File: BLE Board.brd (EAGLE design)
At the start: 160 x 100 mm, 34 parts, among them IC1 TM4C123GH6PM, IC2 TPS6300, J1 SAMTEC-FTSH-105-01-X-DVJ, Q1 NX5032GA

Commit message: First arrangement of components
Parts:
- removed C4: 2.2uF, EE445L:C0402K
- removed J1: SAMTEC-FTSH-105-01-X-DVJ, SAMTEC-FTSH-105-01-X-DV:SAMTEC-FTSH-105-01-X-DV
- removed PC4, PF0, S1: (no value), EE445L:B3F-10XX
- removed Q1: NX5032GA, EE445L:NX5032GA
- removed R6: 10k, EE445L:R0402
- removed U$1: BGM220P, zyongye:BGM220P
- removed U$2: _SWITCH_SPDT_4.7, Z:_SWITCH_SPDT_4.7
- removed U$3: JTAG_SERIAL, Z:JTAG_SERIAL_PTH
- added BLE: BGM220P, zyongye:BGM220P
- added BLE-DEBUG: SAMTEC-FTSH-105-01-X-DVJ, SAMTEC-FTSH-105-01-X-DV:SAMTEC-FTSH-105-01-X-DV
- added C17, C19: 0.1uF, EE445L:C0402K
- added C18-T, C20-T: 4.7uF, EE445L:C0402K
- added C4-T: 2.2uF, EE445L:C0402K
- added CRYS: NX5032GA, EE445L:NX5032GA
- added JTAG: JTAG_SERIAL, Z:JTAG_SERIAL_PTH
- added ON/OFF: _SWITCH_SPDT_4.7, Z:_SWITCH_SPDT_4.7
- added R5: 10k, EE445L:R0402
- added RST, SW-PC4, SW-PF0: (no value), EE445L:B3F-10XX
- C13, C14, C16: value 0.01uF -> 10uF
- C15: value 0.01uF -> 0.1uF
- R3: value 1M -> 100
- moved R4 146.8 mm to (39.1, 49.5), flipped to the bottom
- moved DIS1 104.0 mm to (19.1, 43.2), flipped to the bottom
- moved C9 82.1 mm to (27.4, 25.9), turned to 315 degrees
- moved B1 79.4 mm to (31.0, 7.11), flipped to the bottom
- moved R1 78.4 mm to (39.6, 18.5), flipped to the bottom
- moved C12 75.5 mm to (24.8, 19.2), turned to 45 degrees
- moved C16 73.3 mm to (10.4, 7.37), flipped to the bottom, turned to 90 degrees
- moved C11 72.1 mm to (27.3, 21.7), turned to 225 degrees
- moved IC1 71.1 mm to (17.8, 30.5), turned to 225 degrees
- moved C15 69.2 mm to (11.7, 7.37), flipped to the bottom, turned to 90 degrees
- moved C1 68.7 mm to (8.89, 23.4), turned to 225 degrees
- moved C5 67.7 mm to (10.4, 21.8), turned to 45 degrees
- moved IC2 67.1 mm to (6.86, 3.81), flipped to the bottom, turned to 180 degrees
- moved C3 60.8 mm to (7.37, 24.9), turned to 225 degrees
- moved C14 60.3 mm to (3.30, 4.57), flipped to the bottom
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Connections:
- net +3V3: now also BLE.VDD, C17.2, C18-T.2, C19.1, C20-T.1, JTAG.3V3, SW-PC4.3, SW-PC4.4, SW-PF0.3, SW-PF0.4; no longer PC4.3, PC4.4, PF0.3, PF0.4, U$1.VDD, U$3.3V3
- net BAT: now also ON/OFF.P$2; no longer U$2.P$2
- net BGM_RST: now also BLE-DEBUG.3, BLE.RESET; no longer J1.3, U$1.RESET
- net GND: now also BLE-DEBUG.2, BLE.GND1, BLE.GND2, BLE.GND3, BLE.GND4, C17.1, C18-T.1, C19.2, C20-T.2, C4-T.2, JTAG.GND, R5.2, RST.3, RST.4; no longer C4.2, J1.2, R6.2, S1.3, S1.4, U$1.GND1, U$1.GND2, U$1.GND3, U$1.GND4, U$3.GND
- net IN: now also ON/OFF.P$1; no longer U$2.P$1
- net N$5: now also JTAG.5V; no longer U$3.5V
- net OSC0: now also CRYS.2; no longer Q1.2
- net OSC1: now also CRYS.1; no longer Q1.1
- net PF3: now also R5.1, SW-PF0.1, SW-PF0.2; no longer PF0.1, PF0.2, R6.1
- net PF4: now also SW-PC4.1, SW-PC4.2; no longer PC4.1, PC4.2
- net PTI_DATA: now also BLE-DEBUG.10, BLE.PC4; no longer J1.10, U$1.PC4
- net PTI_FRAME: now also BLE-DEBUG.9, BLE.PC5; no longer J1.9, U$1.PC5
- net RST: now also JTAG.RST, RST.1, RST.2; no longer S1.1, S1.2, U$3.RST
- net RXD: now also JTAG.RXD; no longer U$3.RXD
- net SWCLK: now also BLE-DEBUG.8, BLE.PA1; no longer J1.8, U$1.PA1
- net SWDIO: now also BLE-DEBUG.7, BLE.PA2; no longer J1.7, U$1.PA2
- net SWO: now also BLE-DEBUG.6, BLE.PA3; no longer J1.6, U$1.PA3
- net TCK: now also JTAG.TCK; no longer U$3.TCK
- net TDI: now also JTAG.TDI; no longer U$3.TDI
- net TDO: now also JTAG.TDO; no longer U$3.TDO
- net TMS: now also JTAG.TMS; no longer U$3.TMS
- net TXD: now also JTAG.TXD; no longer U$3.TXD
- net U1CTS: now also BLE.PA7; no longer U$1.PA7
- net U1RTS: now also BLE.PA8; no longer U$1.PA8
- net U1RX: now also BLE.PA5; no longer U$1.PA5
- net U1TX: now also BLE.PA6; no longer U$1.PA6
- net VDD: now also BLE-DEBUG.1; no longer J1.1
- net VDDC: now also C4-T.1; no longer C4.1
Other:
- board size 160 x 100 mm -> 51.3 x 67 mm

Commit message: revised BLE layout
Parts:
- moved BLE-DEBUG 27.7 mm to (-0.76, 52.8), flipped to the bottom
- moved C18-T 22.9 mm to (20.6, 49.8), flipped to the bottom
- moved C17 17.0 mm to (15.2, 49.8), flipped to the bottom
- moved BLE 12.5 mm to (24.4, 59.9), flipped to the bottom, turned to 0 degrees
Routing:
- added copper zone on layer 16, net N$2

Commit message: First traces
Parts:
- moved C17 2.42 mm to (12.8, 49.9)
- moved C18-T 2.42 mm to (23.0, 49.9), turned to 0 degrees
- moved C3 1.48 mm to (8.13, 23.6)
- moved C1 1.48 mm to (9.65, 22.1)
- moved C5 1.31 mm to (11.0, 20.7)
- moved R5 0.85 mm to (39.2, 35.8)
- moved R4 0.65 mm to (39.2, 48.9), turned to 180 degrees
- moved BLE-DEBUG 0.51 mm to (-0.76, 53.3)
- moved L1 0.51 mm to (6.86, 8.13)
- moved R2 0.18 mm to (12.3, 19.7)
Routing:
- net GND: track 0.00 -> 314.2 mm, vias 0 -> 18
- net +3V3: track 0.00 -> 196.1 mm, vias 0 -> 11
- net TXD: track 0.00 -> 70.2 mm
- net RXD: track 0.00 -> 67.8 mm
- net RST: track 0.00 -> 55.9 mm, vias 0 -> 1
- net SWCLK: track 0.00 -> 52.5 mm, vias 0 -> 4
- net BGM_RST: track 0.00 -> 49.8 mm, vias 0 -> 4
- net PF4: track 0.00 -> 48.2 mm, vias 0 -> 3
- net SWO: track 0.00 -> 46.0 mm, vias 0 -> 2
- net SWDIO: track 0.00 -> 43.3 mm, vias 0 -> 2
- net PF3: track 0.00 -> 39.7 mm, vias 0 -> 1
- net TFT_CS: track 0.00 -> 38.6 mm
- net PTI_FRAME: track 0.00 -> 31.8 mm, vias 0 -> 2
- net SCLK: track 0.00 -> 30.0 mm
- net U1CTS: track 0.00 -> 28.4 mm, vias 0 -> 3
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
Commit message: Fix all errors
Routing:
- net N$4: track 3.92 -> 3.34 mm
- removed copper zone on layer 16, net N$2
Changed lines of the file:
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@@
 <hole x="-3.429" y="2.413" drill="1"/>
 <hole x="43.053" y="2.54" drill="1"/>
+<polygon width="0.4064" layer="39">
+<vertex x="14.859" y="65.659"/>
+<vertex x="14.859" y="59.944"/>
+<vertex x="14.986" y="59.817"/>
+<vertex x="21.082" y="59.817"/>
+<vertex x="21.082" y="65.532"/>
+<vertex x="20.955" y="65.659"/>
+</polygon>
 </plain>
 <attributes>
@@
 <wire x1="22.98839375" y1="26.3322625" x2="22.437828125" y2="26.882828125" width="0.2032" layer="1"/>
 <wire x1="22.437828125" y1="26.882828125" x2="22.270125" y2="27.05053125" width="0.2032" layer="1"/>
-<wire x1="22.270125" y1="27.05053125" x2="22.134359375" y2="27.05053125" width="0.2032" layer="1"/>
 <wire x1="6.35" y1="12.7" x2="6.35" y2="13.716" width="0.508" layer="16"/>
 <wire x1="6.35" y1="13.716" x2="10.668" y2="18.034" width="0.508" layer="16"/>
@@
 <wire x1="22.387" y1="49.911" x2="13.427" y2="49.911" width="0.508" layer="16"/>
 <wire x1="13.427" y1="49.911" x2="13.462" y2="49.876" width="0.508" layer="16"/>
-<wire x1="13.462" y1="49.876" x2="13.462" y2="49.2208" width="0.508" layer="16"/>
-<via x="13.462" y="49.2208" extent="1-16" drill="0.381" diameter="0.55"/>
-<wire x1="13.462" y1="49.2208" x2="13.462" y2="41.061471875" width="0.508" layer="1"/>
+<wire x1="13.462" y1="49.876" x2="13.462" y2="48.9668" width="0.508" layer="16"/>
+<via x="13.462" y="48.9668" extent="1-16" drill="0.381" diameter="0.55"/>
+<wire x1="13.462" y1="48.9668" x2="13.462" y2="41.061471875" width="0.508" layer="1"/>
 <wire x1="13.462" y1="41.061471875" x2="11.8542625" y2="39.453734375" width="0.508" layer="1"/>
 <wire x1="21.534" y1="52.324" x2="21.534" y2="50.764" width="0.508" layer="16"/>
@@
 <wire x1="27.8562625" y1="25.5702625" x2="28.448" y2="26.162" width="0.254" layer="1"/>
 <via x="28.448" y="26.162" extent="1-16" drill="0.381" diameter="0.55"/>
-<wire x1="28.448" y1="26.162" x2="27.570328125" y2="27.039671875" width="0.254" layer="16"/>
-<wire x1="27.570328125" y1="27.039671875" x2="20.435671875" y2="27.039671875" width="0.254" layer="16"/>
+<wire x1="28.448" y1="26.162" x2="27.951328125" y2="26.658671875" width="0.254" layer="16"/>
+<wire x1="27.951328125" y1="26.658671875" x2="20.816671875" y2="26.658671875" width="0.254" layer="16"/>
+<wire x1="20.816671875" y1="26.658671875" x2="20.435671875" y2="27.039671875" width="0.254" layer="16"/>
 <via x="20.435671875" y="27.039671875" extent="1-16" drill="0.381" diameter="0.55"/>
 <wire x1="20.435671875" y1="27.039671875" x2="20.435671875" y2="26.830371875" width="0.254" layer="1"/>
@@
 <wire x1="8.382" y1="48.895" x2="9.525" y2="50.038" width="0.508" layer="1"/>
 <wire x1="23.587" y1="49.911" x2="23.622" y2="49.876" width="0.254" layer="16"/>
-<wire x1="23.622" y1="49.876" x2="23.622" y2="49.2208" width="0.254" layer="16"/>
-<via x="23.622" y="49.2208" extent="1-16" drill="0.381" diameter="0.55"/>
-<wire x1="23.622" y1="49.2208" x2="23.622" y2="41.234525" width="0.254" layer="1"/>
+<wire x1="23.622" y1="49.876" x2="23.622" y2="48.9668" width="0.254" layer="16"/>
+<via x="23.622" y="48.9668" extent="1-16" drill="0.381" diameter="0.55"/>
+<wire x1="23.622" y1="48.9668" x2="23.622" y2="41.234525" width="0.254" layer="1"/>
 <wire x1="23.622" y1="41.234525" x2="24.8082625" y2="40.0482625" width="0.254" layer="1"/>
 <wire x1="11.005734375" y1="40.3022625" x2="11.684" y2="40.980528125" width="0.254" layer="1"/>
@@
 <wire x1="39.56145" y1="24.765" x2="38.52805" y2="23.7316" width="0.254" layer="16"/>
 <wire x1="37.67195" y1="23.7316" x2="37.65455" y2="23.749" width="0.254" layer="16"/>
-<via x="22.938740625" y="31.623" extent="1-16" drill="0.381" diameter="0.55"/>
+<via x="22.811740625" y="31.369" extent="1-16" drill="0.381" diameter="0.55"/>
 <wire x1="32.21978125" y1="23.749" x2="28.11630625" y2="27.852475" width="0.254" layer="16"/>
-<wire x1="26.709265625" y1="27.852475" x2="22.938740625" y2="31.623" width="0.254" layer="16"/>
-<wire x1="28.11630625" y1="27.852475" x2="26.709265625" y2="27.852475" width="0.254" layer="16"/>
-<wire x1="22.938740625" y1="31.623" x2="23.08674375" y2="31.771003125" width="0.254" layer="1"/>
-<wire x1="23.08674375" y1="31.771003125" x2="23.08674375" y2="31.7978125" width="0.254" layer="1"/>
-<wire x1="23.08674375" y1="31.7978125" x2="23.684340625" y2="32.395409375" width="0.254" layer="1"/>
-<wire x1="23.684340625" y1="32.395409375" x2="23.684340625" y2="32.495253125" width="0.254" layer="1"/>
+<wire x1="26.328265625" y1="27.852475" x2="22.811740625" y2="31.369" width="0.254" layer="16"/>
+<wire x1="28.11630625" y1="27.852475" x2="26.328265625" y2="27.852475" width="0.254" layer="16"/>
+<wire x1="22.811740625" y1="31.369" x2="22.6713375" y2="31.50940625" width="0.254" layer="1"/>
+<wire x1="23.684340625" y1="32.495253125" x2="23.657184375" y2="32.495253125" width="0.254" layer="1"/>
+<wire x1="23.657184375" y1="32.495253125" x2="22.6713375" y2="31.50940625" width="0.254" layer="1"/>
 <wire x1="37.65455" y1="23.749" x2="32.21978125" y2="23.749" width="0.254" layer="16"/>
 </signal>
@@
 <contactref element="IC1" pad="32"/>
 <contactref element="R2" pad="1"/>
-<wire x1="12.920040625" y1="20.316740625" x2="12.920040625" y2="20.286040625" width="0.2032" layer="1"/>
+<via x="13.589" y="20.955" extent="1-16" drill="0.381" diameter="0.55"/>
 <wire x1="12.920040625" y1="20.286040625" x2="13.589" y2="20.955" width="0.254" layer="1"/>
-<via x="13.589" y="20.955" extent="1-16" drill="0.381" diameter="0.55"/>
-<wire x1="13.589" y1="20.955" x2="15.621" y2="22.987" width="0.254" layer="16"/>
-<via x="15.621" y="22.987" extent="1-16" drill="0.381" diameter="0.55"/>
-<wire x1="15.621" y1="22.987" x2="16.47185" y2="23.83785" width="0.254" layer="1"/>
+<wire x1="15.494" y1="22.86" x2="13.589" y2="20.955" width="0.254" layer="16"/>
+<via x="15.494" y="22.86" extent="1-16" drill="0.381" diameter="0.55"/>
+<wire x1="15.494" y1="22.86" x2="16.47185" y2="23.83785" width="0.254" layer="1"/>
 <wire x1="16.47185" y1="23.83785" x2="16.47185" y2="23.86855" width="0.254" layer="1"/>
 </signal>
@@
 <contactref element="IC2" pad="5"/>
 <contactref element="ON/OFF" pad="P$1"/>
-<wire x1="7.858" y1="5.285" x2="9.535" y2="5.285" width="0.508" layer="16"/>
-<wire x1="9.535" y1="5.285" x2="10.16" y2="4.66" width="0.508" layer="16"/>
-<wire x1="10.16" y1="4.66" x2="14.77" y2="4.66" width="0.508" layer="16"/>
+<wire x1="10.16" y1="4.66" x2="12.192" y2="4.66" width="0.508" layer="16"/>
+<wire x1="12.192" y1="4.66" x2="14.77" y2="4.66" width="0.508" layer="16"/>
 <wire x1="14.77" y1="4.66" x2="15.366" y2="4.064" width="0.508" layer="16"/>
 <wire x1="10.414" y1="6.766" x2="10.414" y2="4.914" width="0.508" layer="16"/>
 <wire x1="10.414" y1="4.914" x2="10.16" y2="4.66" width="0.508" layer="16"/>
+<wire x1="10.16" y1="4.66" x2="9.535" y2="5.285" width="0.4064" layer="16"/>
+<wire x1="9.535" y1="5.285" x2="7.858" y2="5.285" width="0.4064" layer="16"/>
 </signal>
 <signal name="N$1">
@@
 <contactref element="L1" pad="2"/>
 <contactref element="IC2" pad="2"/>
-<wire x1="6.329" y1="7.641" x2="5.842" y2="8.128" width="0.2032" layer="16"/>
-<wire x1="5.842" y1="8.128" x2="5.715" y2="8.255" width="0.2032" layer="16"/>
-<wire x1="6.329" y1="7.641" x2="6.329" y2="5.314" width="0.2032" layer="16"/>
+<wire x1="5.158" y1="8.128" x2="6.329" y2="6.957" width="0.2032" layer="16"/>
+<wire x1="6.329" y1="6.957" x2="6.329" y2="5.314" width="0.2032" layer="16"/>
 <wire x1="6.329" y1="5.314" x2="6.358" y2="5.285" width="0.2032" layer="16"/>
-<wire x1="5.158" y1="8.128" x2="5.842" y2="8.128" width="0.2032" layer="16"/>
 </signal>
 <signal name="MISO">
@@
 <wire x1="25.794" y1="54.724" x2="27.051" y2="53.467" width="0.3048" layer="16"/>
 <wire x1="27.051" y1="53.467" x2="27.051" y2="51.181" width="0.3048" layer="16"/>
-<wire x1="27.051" y1="51.181" x2="24.511" y2="48.641" width="0.3048" layer="16"/>
-<wire x1="24.511" y1="48.641" x2="11.684" y2="48.641" width="0.3048" layer="16"/>
-<wire x1="11.684" y1="48.641" x2="8.001" y2="52.324" width="0.3048" layer="16"/>
+<wire x1="27.051" y1="51.181" x2="24.257" y2="48.387" width="0.3048" layer="16"/>
+<wire x1="24.257" y1="48.387" x2="11.938" y2="48.387" width="0.3048" layer="16"/>
+<wire x1="11.938" y1="48.387" x2="8.001" y2="52.324" width="0.3048" layer="16"/>
 <wire x1="8.001" y1="52.324" x2="8.001" y2="52.451" width="0.3048" layer="16"/>
 <wire x1="8.001" y1="58.039" x2="8.001" y2="58.166" width="0.3048" layer="16"/>
@@
 <wire x1="38.1" y1="22.225" x2="30.607" y2="14.732" width="0.2032" layer="1"/>
 <wire x1="30.607" y1="14.732" x2="30.607" y2="10.414" width="0.2032" layer="1"/>
-<wire x1="30.607" y1="10.414" x2="27.94" y2="7.747" width="0.2032" layer="1"/>
-<wire x1="27.94" y1="7.747" x2="6.223" y2="7.747" width="0.2032" layer="1"/>
-<wire x1="6.223" y1="7.747" x2="2.159" y2="11.811" width="0.2032" layer="1"/>
-<wire x1="2.159" y1="11.811" x2="2.159" y2="25.146" width="0.2032" layer="1"/>
+<wire x1="30.607" y1="10.414" x2="27.559" y2="7.366" width="0.2032" layer="1"/>
+<wire x1="27.559" y1="7.366" x2="7.112" y2="7.366" width="0.2032" layer="1"/>
+<wire x1="7.112" y1="7.366" x2="2.159" y2="12.319" width="0.2032" layer="1"/>
+<wire x1="2.159" y1="12.319" x2="2.159" y2="25.146" width="0.2032" layer="1"/>
 <wire x1="9.9367" y1="27.94" x2="11.16855" y2="29.17185" width="0.2032" layer="1"/>
 <wire x1="2.159" y1="25.146" x2="4.953" y2="27.94" width="0.2032" layer="1"/>
 <wire x1="4.953" y1="27.94" x2="9.9367" y2="27.94" width="0.2032" layer="1"/>
 </signal>
-<signal name="N$2">
-<polygon width="0.1524" layer="16">
-<vertex x="14.478" y="66.802"/>
-<vertex x="14.478" y="59.436"/>
-<vertex x="21.59" y="59.436"/>
-<vertex x="21.59" y="67.056"/>
-<vertex x="21.336" y="66.802"/>
-</polygon>
-</signal>
 </signals>

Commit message: Add label
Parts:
- added U$1: (no value), Z:__LOGO_UT_ECE
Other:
- board text added: "UT Austin EE445L Yongye Zhu Benjamin Fa Melissa Yang Faiyaz Mostofa"
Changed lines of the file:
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@@
 <drawing>
 <settings>
-<setting alwaysvectorfont="no"/>
+<setting alwaysvectorfont="yes"/>
 <setting verticaltext="up"/>
 </settings>
@@
 <layer number="19" name="Unrouted" color="6" fill="1" visible="yes" active="yes"/>
 <layer number="20" name="Dimension" color="24" fill="1" visible="yes" active="yes"/>
-<layer number="21" name="tPlace" color="7" fill="1" visible="no" active="yes"/>
-<layer number="22" name="bPlace" color="7" fill="1" visible="no" active="yes"/>
+<layer number="21" name="tPlace" color="7" fill="1" visible="yes" active="yes"/>
+<layer number="22" name="bPlace" color="7" fill="1" visible="yes" active="yes"/>
 <layer number="23" name="tOrigins" color="15" fill="1" visible="yes" active="yes"/>
 <layer number="24" name="bOrigins" color="15" fill="1" visible="yes" active="yes"/>
 <layer number="25" name="tNames" color="7" fill="1" visible="no" active="yes"/>
 <layer number="26" name="bNames" color="7" fill="1" visible="no" active="yes"/>
-<layer number="27" name="tValues" color="7" fill="1" visible="no" active="yes"/>
+<layer number="27" name="tValues" color="7" fill="1" visible="yes" active="yes"/>
 <layer number="28" name="bValues" color="7" fill="1" visible="no" active="yes"/>
 <layer number="29" name="tStop" color="7" fill="3" visible="no" active="yes"/>
@@
 <vertex x="20.955" y="65.659"/>
 </polygon>
+<text x="0.635" y="36.1188" size="1.2" layer="21" rot="R271.1" align="center">UT Austin
+EE445L
+Yongye Zhu
+Benjamin Fa
+Melissa Yang
+Faiyaz Mostofa</text>
 </plain>
 <attributes>
@@
 <attribute name="VALUE" x="23.487" y="48.461" size="1.016" layer="28" rot="MR0"/>
 </element>
+<element name="U$1" library="Z" package="__LOGO_UT_ECE" value="" x="-0.762" y="40.767" smashed="yes" rot="MR270"/>
 </elements>
 <signals>
@@
 </drawing>
 <compatibility>
+<note version="6.3" minversion="6.2.2" severity="warning">
+Since Version 6.2.2 text objects can contain more than one line,
+which will not be processed correctly with this version.
+</note>
 <note version="8.2" severity="warning">
 Since Version 8.2, EAGLE supports online libraries. The ids

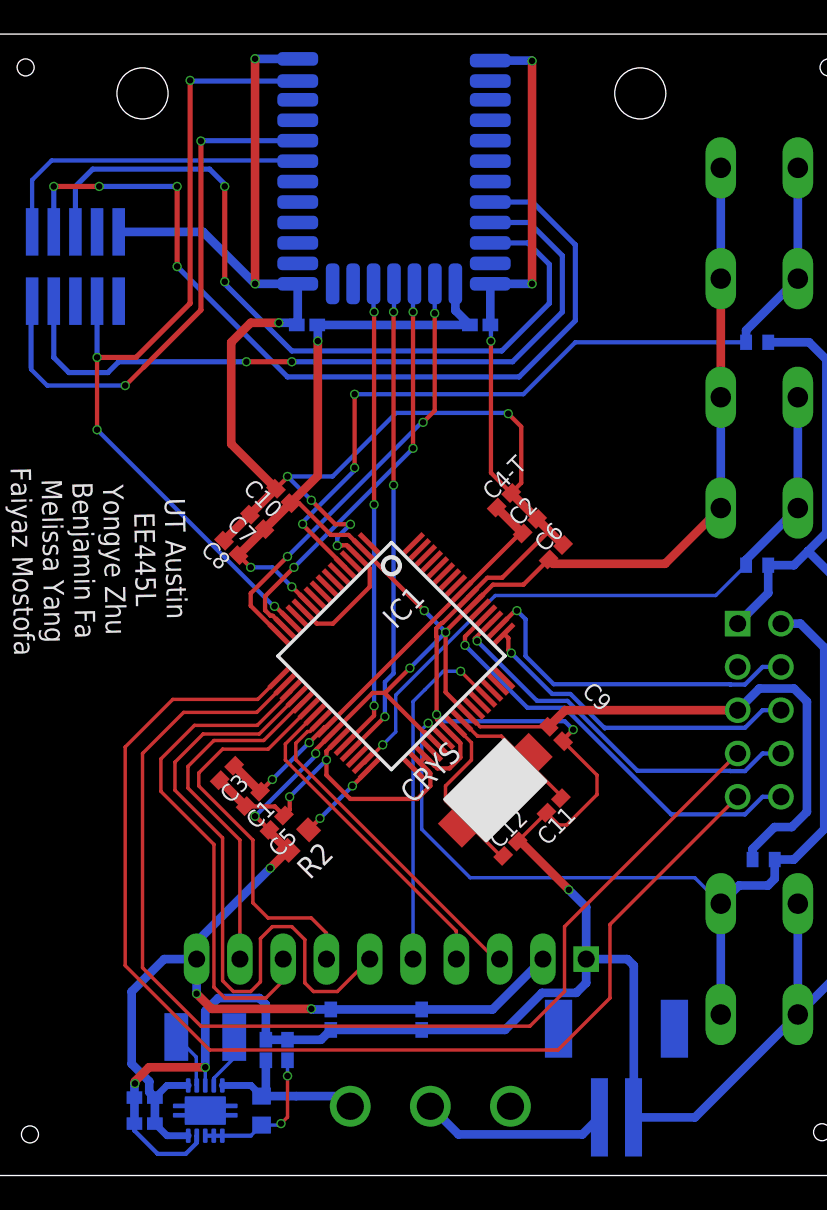
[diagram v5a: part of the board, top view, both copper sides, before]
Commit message: Flip the LCD
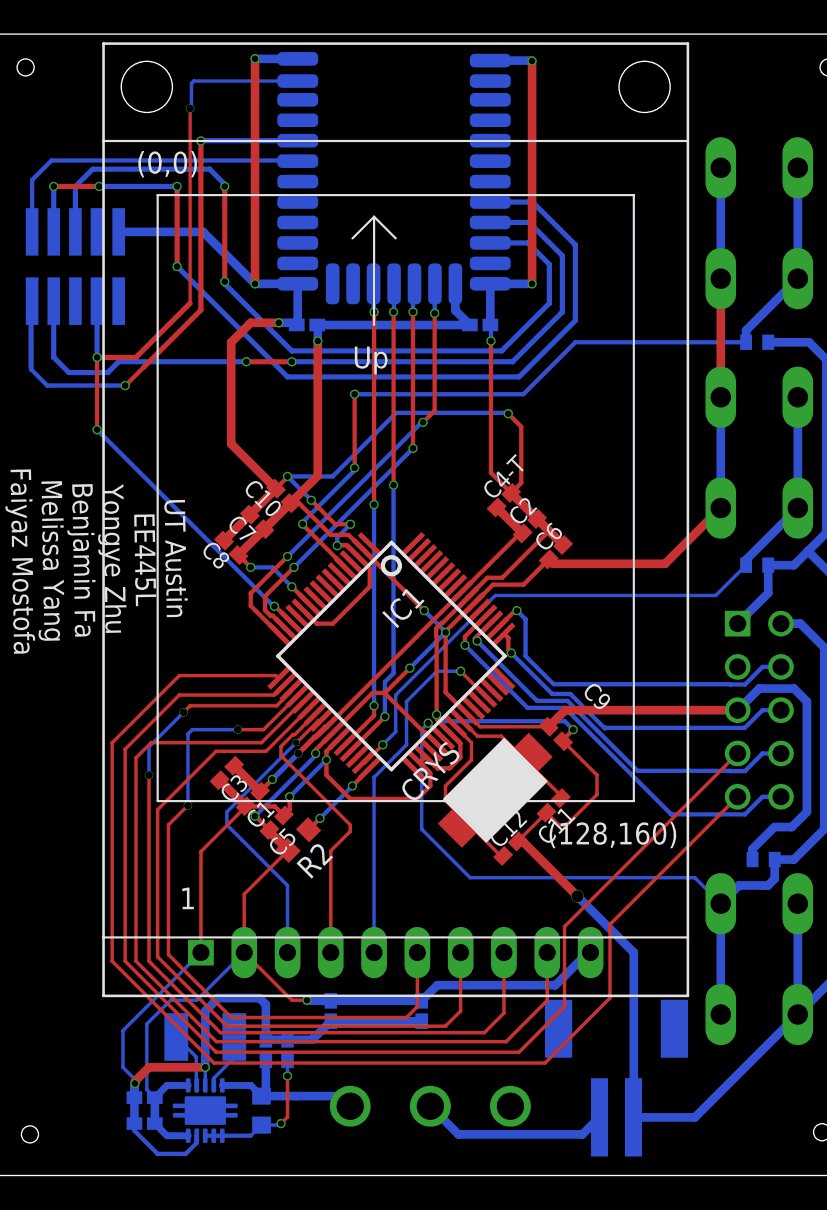
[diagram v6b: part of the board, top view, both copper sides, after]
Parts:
- moved DIS1 2.32 mm to (16.8, 43.6), flipped to the top
- moved C19 0.51 mm to (19.6, 9.65)
- moved C20-T 0.51 mm to (14.2, 9.65)
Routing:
- net MISO: track 20.9 -> 53.0 mm
- net MOSI: track 23.5 -> 43.2 mm
- net SCLK: track 30.0 -> 48.9 mm, vias 0 -> 2
- net GND: track 314.2 -> 320.7 mm
- net RXD: track 67.8 -> 71.5 mm
- net RESET: track 19.8 -> 17.5 mm, vias 0 -> 1
- net TXD: track 70.2 -> 72.5 mm
- net +3V3: track 196.0 -> 193.7 mm, vias 11 -> 9
- net C/D: track 19.2 -> 17.0 mm
- net TFT_CS: track 38.6 -> 40.3 mm, vias 0 -> 2
- net SD_CS: track 20.7 -> 21.5 mm
